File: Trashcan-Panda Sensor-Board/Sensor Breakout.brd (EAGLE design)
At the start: 21.8 x 21.8 mm, 14 parts, among them J6 BM06B-SRSS-TBT(LF)(SN), U2 VL53L1X

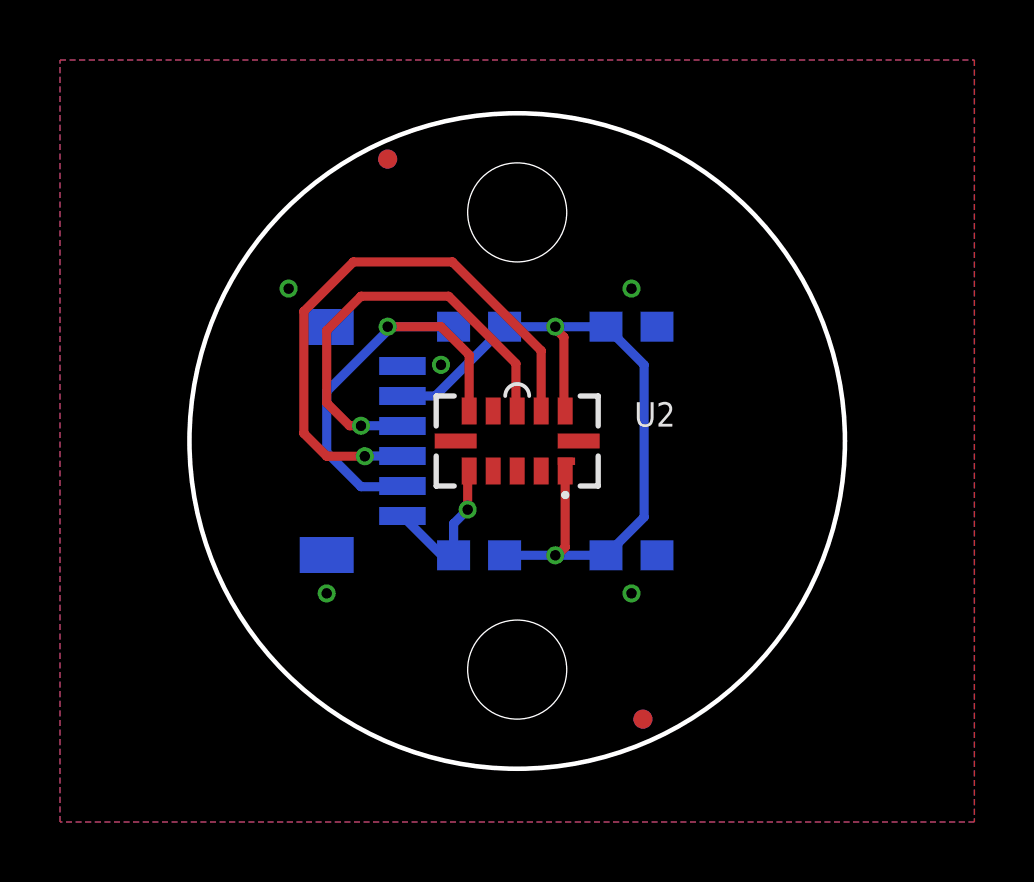
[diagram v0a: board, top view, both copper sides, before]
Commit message: Rectangular Sensor Board
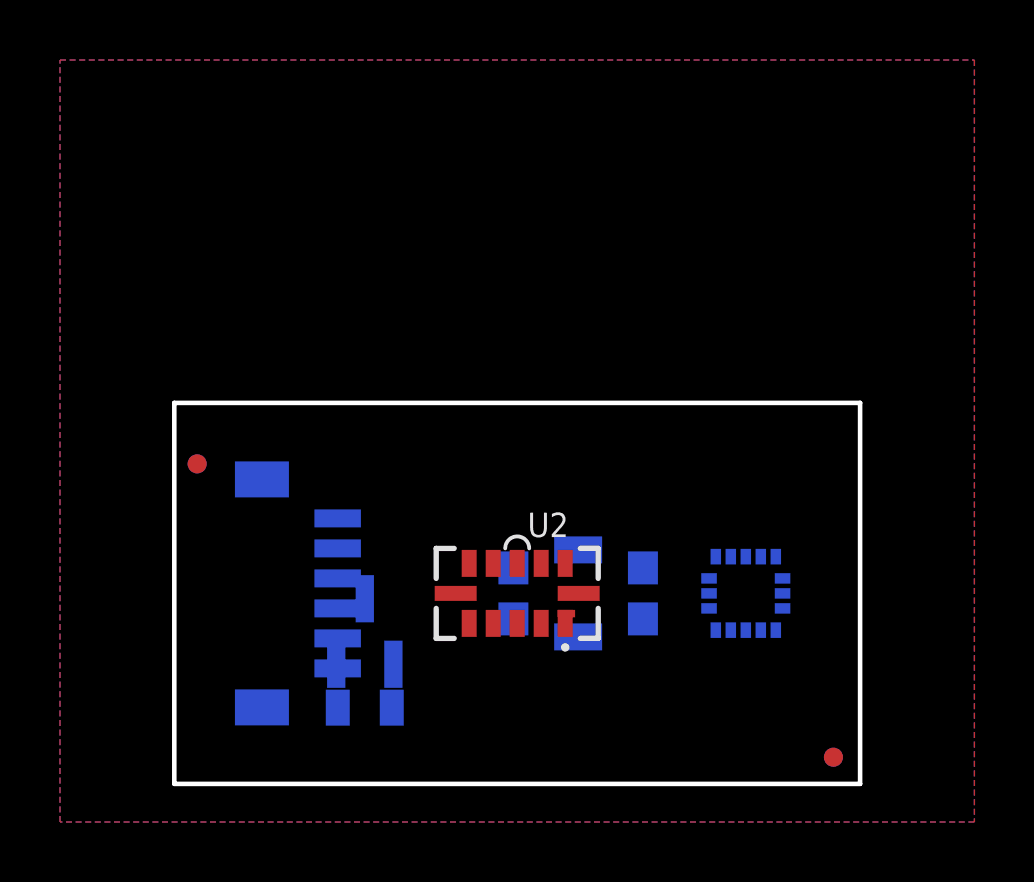
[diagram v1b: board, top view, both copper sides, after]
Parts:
- removed C1: 4.7uF, SparkFun-Capacitors:0603
- removed JP3, JP4: STAND-OFF, SparkFun:STAND-OFF
- removed R1: 10k, SparkFun-Resistors:0603
- added C3: (no value), Custom Components:C1206
- added Q1: BSS215P, Custom Components:SOT-23_3L_ONS-M
- added R4: 100k, Custom Components:0805
- added U1: LIS3DH, Custom Components:PQFN50P300X300X100-16N
- moved LOGO1 30.2 mm to (24.6, 27.8)
- moved JP1 12.0 mm to (0.76, 10.7)
- moved JP6 12.0 mm to (0.76, 10.7)
- moved C4 8.90 mm to (15.6, 6.35), turned to 270 degrees
- moved JP2 6.48 mm to (22.0, 0.89)
- moved JP5 6.48 mm to (22.0, 0.89)
- moved J6 5.52 mm to (2.92, 6.35)
- moved U2 5.08 mm to (11.4, 6.35)
- moved R2 1.71 mm to (11.3, 6.35), turned to 90 degrees
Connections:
- removed net !INT: J6.5, R1.1, U2.7
- new net !EN: J6.6, Q1.1, R4.1
- new net INT: J6.5, U1.11
- new net RES: U1.10
- new net VCC-IN: J6.2, Q1.2, R4.2
- net !SHUT: no longer J6.6
- net GND: now also C3.P$2, U1.12, U1.5; no longer C1.2
- net SCL: now also U1.4
- net SDA: now also U1.6
- net VCC: now also C3.P$1, Q1.3, U1.1, U1.14; no longer C1.1, J6.2, R1.2
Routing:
- net VCC: track 25.7 -> 0.00 mm, vias 2 -> 0
- net SCL: track 19.5 -> 0.00 mm, vias 1 -> 0
- net !INT: track 15.2 -> 0.00 mm, vias 1 -> 0
- net SDA: track 14.6 -> 0.00 mm, vias 1 -> 0
- net !SHUT: track 5.27 -> 0.00 mm, vias 1 -> 0
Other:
- board size 21.8 x 21.8 mm -> 22.9 x 12.7 mm

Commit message: Updated battery board to v1.1
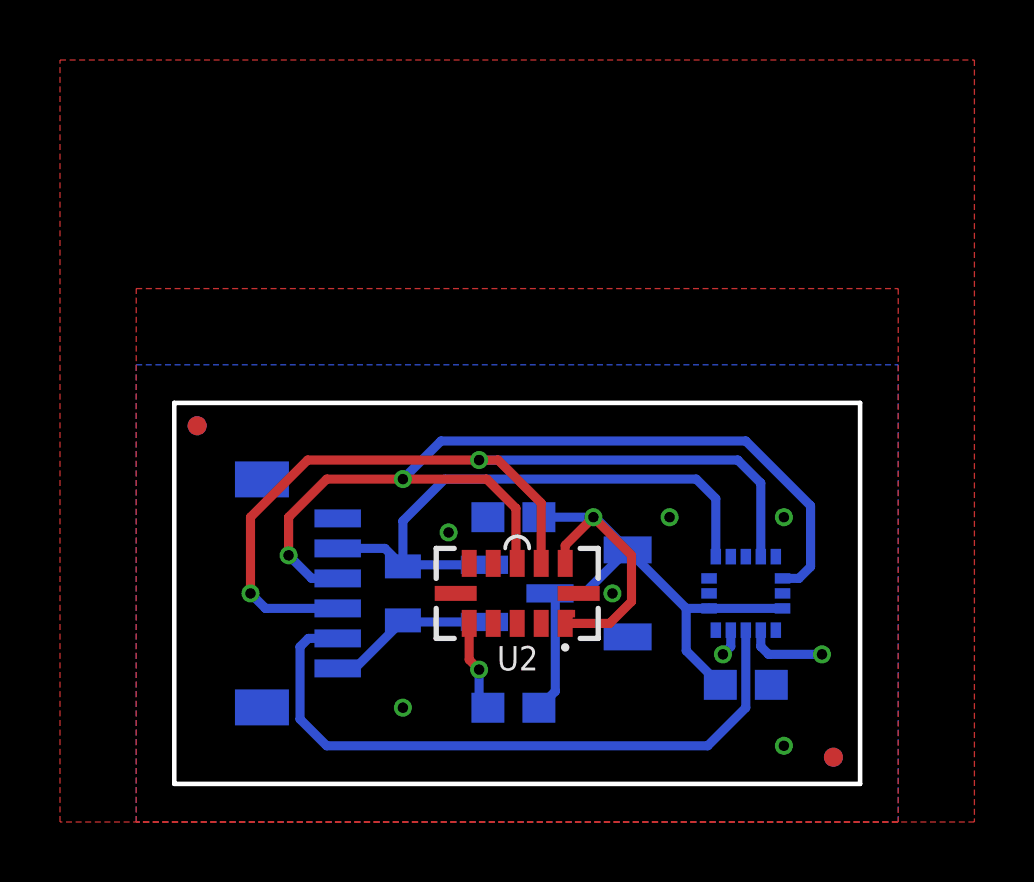
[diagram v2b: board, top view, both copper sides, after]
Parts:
- removed C4: 0.1uF, SparkFun-Capacitors:0603
- removed R4: 100k, Custom Components:0805
- added C1: 10uF, Custom Components:C1206
- added C2: 0.1uF, SparkFun-Capacitors:0603
- added R1: 100k, Custom Components:0805
- C3: value (none) -> 0.1uF; device Custom Components:C1206 -> SparkFun-Capacitors:0603
- moved LOGO1 30.5 mm to (7.62, 2.54)
- moved C3 6.37 mm to (19.1, 3.30), turned to 180 degrees
- moved Q1 5.24 mm to (11.4, 6.35), turned to 90 degrees
- moved R2 3.81 mm to (11.3, 2.54), turned to 180 degrees
- moved JP1 1.27 mm to (0.76, 11.9)
- moved JP6 1.27 mm to (0.76, 11.9)
- renumbered J6 to J1
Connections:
- removed net RES: U1.10
- net !EN: now also R1.1; no longer R4.1
- net GND: now also C1.P$2, C2.2, C3.2, U1.10; no longer C3.P$2, C4.2
- net VCC: now also C1.P$1, C2.1, C3.1, U1.8; no longer C3.P$1, C4.1, U1.1
- net VCC-IN: now also R1.2, U1.1; no longer R4.2
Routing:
- net SDA: track 0.00 -> 31.7 mm, vias 0 -> 2
- net SCL: track 0.00 -> 30.9 mm, vias 0 -> 2
- net VCC: track 0.00 -> 27.4 mm, vias 0 -> 1
- net INT: track 0.00 -> 22.1 mm
- net VCC-IN: track 0.00 -> 19.9 mm
- net !EN: track 0.00 -> 5.58 mm
- net GND: track 0.00 -> 3.61 mm, vias 0 -> 8
- net !SHUT: track 0.00 -> 3.07 mm, vias 0 -> 1
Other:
- board text added: "Sensor Breakout chip@seeinsights.com 2-23-22 v1.0"
- board text removed: "TOF Sensor chip@seeinsights.com 1-10-22 v1.0"

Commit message: Updated - Grounded address pin
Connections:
- net GND: now also U1.7
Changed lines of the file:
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@@
 <wire x1="18.55" y1="5.125" x2="18.55" y2="4.58" width="0.3048" layer="16"/>
 <wire x1="18.55" y1="4.58" x2="18.288" y2="4.318" width="0.3048" layer="16"/>
+<contactref element="U1" pad="7"/>
+<wire x1="20.05" y1="7.575" x2="20.32" y2="8.89" width="0" layer="19" extent="16-16"/>
+<wire x1="20.275" y1="6.35" x2="20.05" y2="7.575" width="0" layer="19" extent="16-16"/>
+<wire x1="19.55" y1="5.125" x2="20.275" y2="6.35" width="0" layer="19" extent="16-16"/>
+<wire x1="18.55" y1="5.125" x2="19.55" y2="5.125" width="0" layer="19" extent="16-16"/>
+<wire x1="19.9" y1="3.302" x2="19.55" y2="5.125" width="0" layer="19" extent="16-16"/>
+<wire x1="20.32" y1="1.27" x2="19.9" y2="3.302" width="0" layer="19" extent="16-16"/>
+<wire x1="15.113" y1="4.9" x2="18.288" y2="4.318" width="0" layer="19" extent="16-16"/>
+<wire x1="14.605" y1="6.35" x2="15.113" y2="4.9" width="0" layer="19" extent="16-16"/>
+<wire x1="13.48" y1="6.35" x2="14.605" y2="6.35" width="0" layer="19" extent="1-1"/>
+<wire x1="12.23" y1="5.35" x2="13.48" y2="6.35" width="0" layer="19" extent="1-1"/>
+<wire x1="11.43" y1="5.35" x2="12.23" y2="5.35" width="0" layer="19" extent="1-1"/>
+<wire x1="10.63" y1="5.35" x2="11.43" y2="5.35" width="0" layer="19" extent="1-1"/>
+<wire x1="9.38" y1="6.35" x2="10.63" y2="5.35" width="0" layer="19" extent="1-1"/>
+<wire x1="9.144" y1="8.382" x2="9.38" y2="6.35" width="0" layer="19" extent="1-1"/>
+<wire x1="10.453" y1="8.89" x2="9.144" y2="8.382" width="0" layer="19" extent="16-16"/>
+<wire x1="16.51" y1="8.89" x2="14.605" y2="6.35" width="0" layer="19" extent="1-1"/>
+<wire x1="5.446" y1="8.85" x2="9.144" y2="8.382" width="0" layer="19" extent="16-16"/>
+<wire x1="2.921" y1="10.15" x2="5.446" y2="8.85" width="0" layer="19" extent="16-16"/>
+<wire x1="7.62" y1="2.54" x2="10.63" y2="5.35" width="0" layer="19" extent="1-1"/>
+<wire x1="2.921" y1="2.55" x2="7.62" y2="2.54" width="0" layer="19" extent="16-16"/>
 </signal>
 <signal name="SCL">

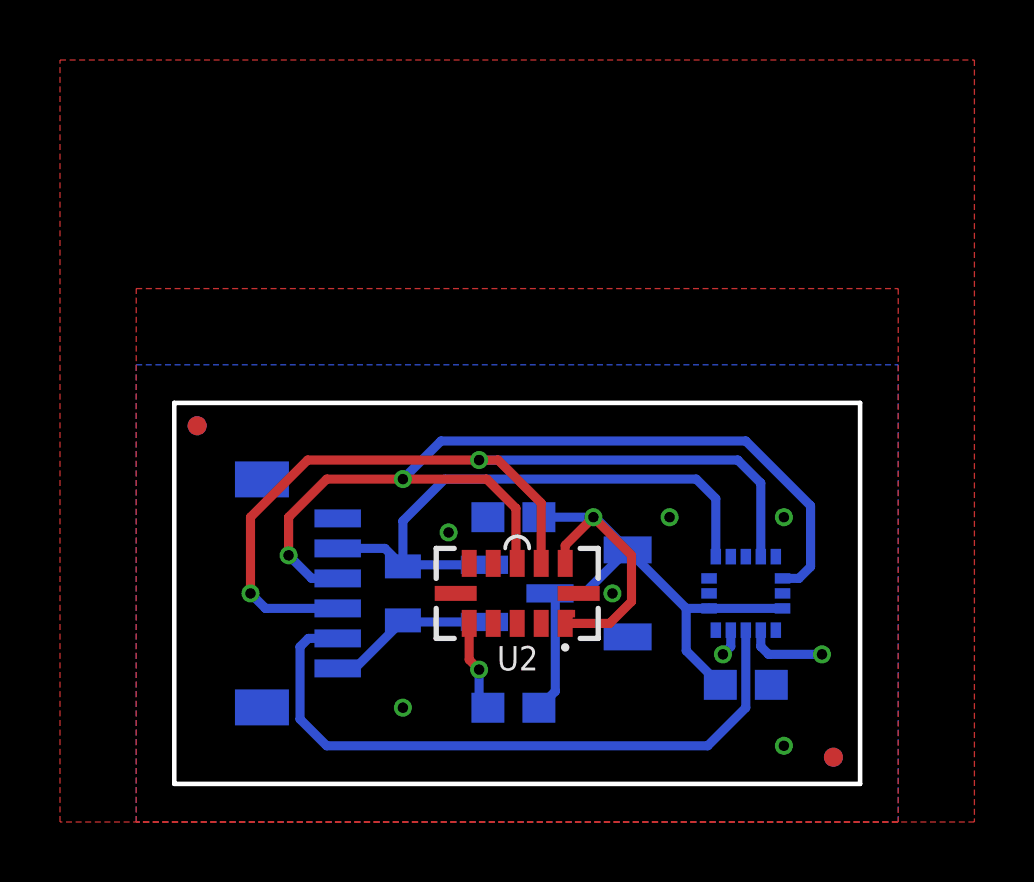
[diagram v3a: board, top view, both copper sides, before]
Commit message: Updated for Macrofab house parts
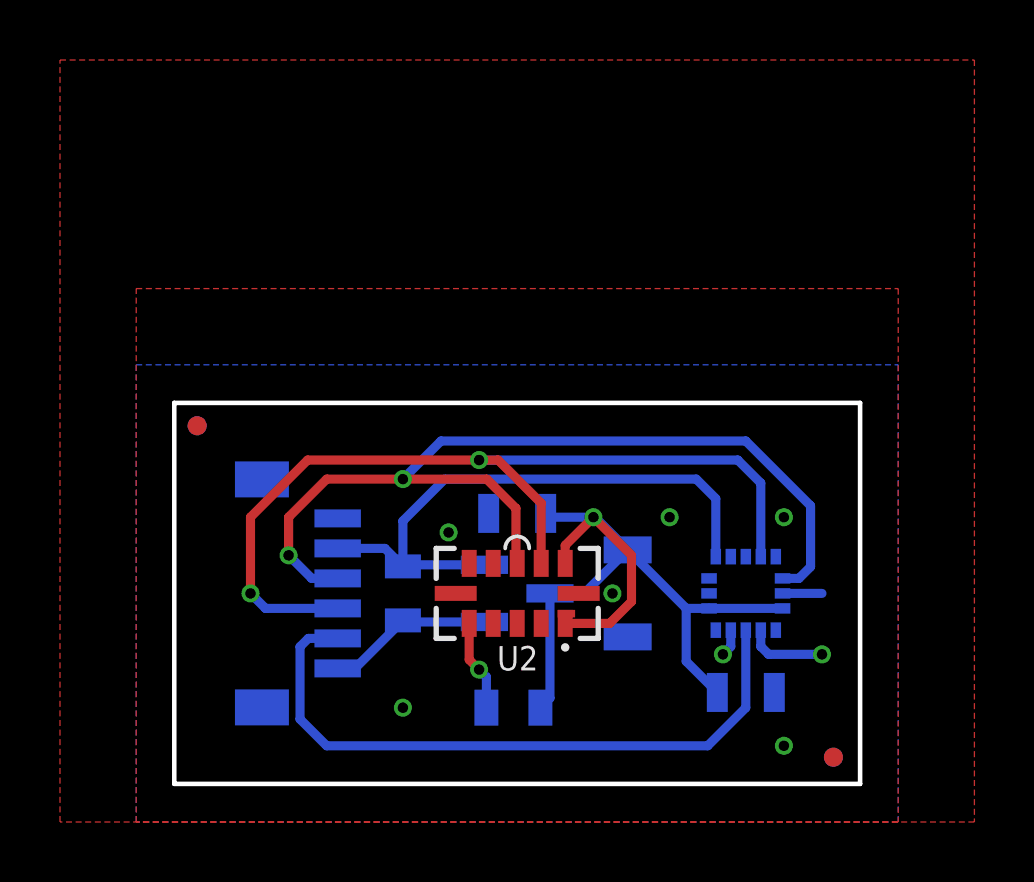
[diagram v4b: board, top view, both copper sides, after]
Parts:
- C2, C3: device SparkFun-Capacitors:0603 -> Custom Components:C0805
- R2: device SparkFun-Resistors:0603 -> Custom Components:0805
- U1: value LIS3DH -> LIS3DHTR
- U2: value VL53L1X -> VL53L1CXV0FY/1
- moved C3 0.25 mm to (19.1, 3.05)
- moved C2 0.18 mm to (11.4, 9.02)
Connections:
- net GND: now also C2.P$2, C3.P$2; no longer C2.2, C3.2
- net VCC: now also C2.P$1, C3.P$1; no longer C2.1, C3.1
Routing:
- net GND: track 3.61 -> 4.92 mm
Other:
- board text added: "Sensor Breakout chip@seeinsights.com 2-23-22 v1.1"
- board text removed: "Sensor Breakout chip@seeinsights.com 2-23-22 v1.0"

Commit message: Added PTC
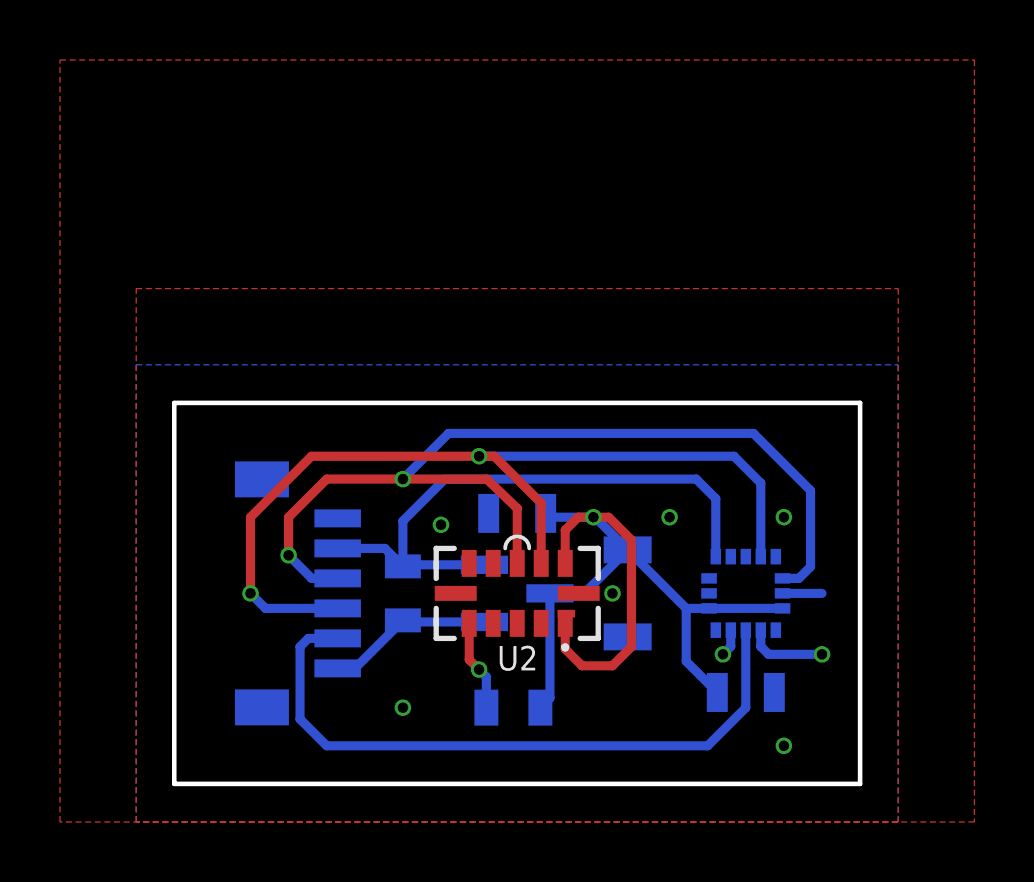
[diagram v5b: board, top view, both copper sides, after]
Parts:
- removed JP1, JP2, JP5, JP6: FIDUCIALUFIDUCIAL, SparkFun:MICRO-FIDUCIAL
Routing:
- net VCC: track 27.4 -> 30.4 mm
- net SDA: track 31.7 -> 32.2 mm
